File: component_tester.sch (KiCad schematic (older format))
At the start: 71 parts, among them IC1 ATMEGA16U2, IC2 ATMEGA328P-A, P1 USB_OTG, P10 BO_PC5, P11 ICSP_prog_328p, P12 CONN_01X01, P13 Device Under Test, P2 BATTERY_CONNECTOR, P3 Voltage_for_zener, P4 ICSP_prog_16u2, P5 BO_PC7, P6 BO_PD0, P7 BO_PD1, P8 BO_PC4, P9 BO_PC6, Q1 TRANSISTOR_NPN_2N2222_KSP222A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, SW1 SWITCH_DPDT_GROUNDED_BODY, SW2 DO_MEASUREMENT, SW3 CONNECT_CAP, U1 NCP1117ST50T3G, U2 XF2L-2625-1A, U3 CDSOT23-SRV05-4, U4 LT1004, Y1 8MHz, Y2 16MHz

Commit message: PCB drawn
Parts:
- removed C12: 100n, Capacitors_SMD:C_0805_HandSoldering, symbol C
- added F1, F2: FUSE, Resistors_SMD:R_0805_HandSoldering, symbol FUSE
- added P12: BO_PD2, Pin_Headers:Pin_Header_Straight_1x01, symbol CONN_01X01
- added P13: BO_PD3, Pin_Headers:Pin_Header_Straight_1x01, symbol CONN_01X01
- added P14: BO_PD4, Pin_Headers:Pin_Header_Straight_1x01, symbol CONN_01X01
- added P15: BO_PD5, Pin_Headers:Pin_Header_Straight_1x01, symbol CONN_01X01
- added P16: BO_PD6, Pin_Headers:Pin_Header_Straight_1x01, symbol CONN_01X01
- D1, D2: footprint Diodes_SMD:SOD-323 -> TO_SOT_Packages_SMD:SOT-23
- D3: renamed from D4; footprint Diodes_SMD:SOD-323 -> TO_SOT_Packages_SMD:SOT-23
- D4: renamed from D5; footprint Diodes_SMD:SOD-323 -> TO_SOT_Packages_SMD:SOT-23
- D7: renamed from D6; footprint Diodes_SMD:SOD-323 -> TO_SOT_Packages_SMD:SOT-23
- SW1: value SWITCH_DPDT_GROUNDED_BODY -> ON-OFF switch
- renumbered C6 to C11, C17 to C16, C18 to C17, C19 to C18, C16 to C19, C8 to C4, C4 to C5, C5 to C6, C11 to C8, D3 to D5, D7 to D6, P12 to P17, P13 to P18, R15 to R14, R14 to R15, R17 to R16, R16 to R17, R6 to R3, R3 to R4, R4 to R5, R5 to R6, U4 to U3, U3 to U4
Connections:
- net 5Volt_328: now also F1.2; no longer SW1.1
- net Battery_input: now also SW1.5, F2.2; no longer C8.1, D3.1 (K), D4.1 (K), R1.1, SW1.6
- net GND: now also C16.1, C17.1, C8.2, D4.2 (A)
- net USB_Vcc: now also SW1.3; no longer SW1.2
- net Volt_reg_5v: now also SW1.2; no longer SW1.3
- net control-niet_data-wel: now also IC1.12 ((~RTS~/AIN5/INT6)PD6); no longer IC1.10 ((INT5/AIN3)PD4)
- net lcd_reset-niet: now also IC1.10 ((INT5/AIN3)PD4); no longer IC1.12 ((~RTS~/AIN5/INT6)PD6)
- net at IC2.1 ((PCINT19/OC2B/INT1)PD3): now also P13.1 (P1)
- net at IC2.10 ((PCINT22/OC0A/AIN0)PD6): now also P16.1 (P1)
- net at IC2.2 ((PCINT20/XCK/T0)PD4): now also P14.1 (P1)
- net at IC2.32 ((PCINT18/INT0)PD2): now also P12.1 (P1)
- net at IC2.9 ((PCINT21/OC0B/T1)PD5): now also P15.1 (P1)
- net Batt_Switch: now reaches C5.1, SW1.4, U1.3 (VI)
- net Batt_Switch: now also R1.1
- new net: F1.1, SW1.1
- new net: C8.1, D3.1 (K), D4.1 (K), F2.1
- no-connect marks 16 -> 11
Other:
- note added: "Optional battery charging circuit"
- note added: "Over voltage protection for test pins"
- moved on the sheet: C11, C19, C4, C8, D3, D4, D6, D7, L1, Q1, R1, R15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

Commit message: Updated schematic. New PCB layout.
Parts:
- added P19: DUT_SMD_1_2, Resistors_Universal:Resistor_SMDuniversal_0805to2512_HandSoldering, symbol CONN_01X02
- added P20: DUT_SMD_2_3, Resistors_Universal:Resistor_SMDuniversal_0805to2512_HandSoldering, symbol CONN_01X02
- C18: footprint Capacitors_SMD:C_0805_HandSoldering -> Capacitors_ThroughHole:C_Disc_D3_P2.5
- P18: footprint Pin_Headers:Pin_Header_Straight_1x03 -> drawn_by_jpmeijers:CONN_DUT
- R11, R12, R13, R14, R16, R18: footprint Resistors_SMD:R_0805_HandSoldering -> Resistors_ThroughHole:Resistor_Horizontal_RM10mm
- Y1, Y2: footprint Crystals:Crystal_HC49-U_Vertical -> Crystals:Crystal_HC49-SD_SMD
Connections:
- net DUT1: now also P19.2 (P2)
- net DUT2: now also P19.1 (P1), P20.2 (P2)
- net DUT3: now also P20.1 (P1)
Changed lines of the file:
@@
 F 0 "P18" H 13050 5000 50  0000 C CNN
 F 1 "Device Under Test" V 13150 4800 50  0000 C CNN
-F 2 "Pin_Headers:Pin_Header_Straight_1x03" H 13050 4800 50  0001 C CNN
+F 2 "drawn_by_jpmeijers:CONN_DUT" H 13050 4800 50  0001 C CNN
 F 3 "" H 13050 4800 50  0000 C CNN
 	1    13050 4800
@@
 F 0 "R11" V 10830 3850 50  0000 C CNN
 F 1 "680" V 10750 3850 50  0000 C CNN
-F 2 "Resistors_SMD:R_0805_HandSoldering" V 10680 3850 50  0001 C CNN
+F 2 "Resistors_ThroughHole:Resistor_Horizontal_RM10mm" V 10680 3850 50  0001 C CNN
 F 3 "" H 10750 3850 50  0000 C CNN
 	1    10750 3850
@@
 F 0 "R12" V 10925 3950 50  0000 C CNN
 F 1 "470k" V 11000 3950 50  0000 C CNN
-F 2 "Resistors_SMD:R_0805_HandSoldering" V 10930 3950 50  0001 C CNN
+F 2 "Resistors_ThroughHole:Resistor_Horizontal_RM10mm" V 10930 3950 50  0001 C CNN
 F 3 "" H 11000 3950 50  0000 C CNN
 	1    11000 3950
@@
 F 0 "R14" V 11580 4150 50  0000 C CNN
 F 1 "470k" V 11500 4150 50  0000 C CNN
-F 2 "Resistors_SMD:R_0805_HandSoldering" V 11430 4150 50  0001 C CNN
+F 2 "Resistors_ThroughHole:Resistor_Horizontal_RM10mm" V 11430 4150 50  0001 C CNN
 F 3 "" H 11500 4150 50  0000 C CNN
 	1    11500 4150
@@
 F 0 "R13" V 11330 4050 50  0000 C CNN
 F 1 "680" V 11250 4050 50  0000 C CNN
-F 2 "Resistors_SMD:R_0805_HandSoldering" V 11180 4050 50  0001 C CNN
+F 2 "Resistors_ThroughHole:Resistor_Horizontal_RM10mm" V 11180 4050 50  0001 C CNN
 F 3 "" H 11250 4050 50  0000 C CNN
 	1    11250 4050
@@
 F 0 "R16" V 11830 4250 50  0000 C CNN
 F 1 "680" V 11750 4250 50  0000 C CNN
-F 2 "Resistors_SMD:R_0805_HandSoldering" V 11680 4250 50  0001 C CNN
+F 2 "Resistors_ThroughHole:Resistor_Horizontal_RM10mm" V 11680 4250 50  0001 C CNN
 F 3 "" H 11750 4250 50  0000 C CNN
 	1    11750 4250
@@
 F 0 "R18" V 12080 4350 50  0000 C CNN
 F 1 "470k" V 12000 4350 50  0000 C CNN
-F 2 "Resistors_SMD:R_0805_HandSoldering" V 11930 4350 50  0001 C CNN
+F 2 "Resistors_ThroughHole:Resistor_Horizontal_RM10mm" V 11930 4350 50  0001 C CNN
 F 3 "" H 12000 4350 50  0000 C CNN
 	1    12000 4350
@@
 F 0 "Y2" V 10775 4400 50  0000 C CNN
 F 1 "16MHz" V 10700 4350 50  0000 C CNN
-F 2 "Crystals:Crystal_HC49-U_Vertical" H 10750 4525 50  0001 C CNN
+F 2 "Crystals:Crystal_HC49-SD_SMD" H 10750 4525 50  0001 C CNN
 F 3 "" H 10750 4525 50  0000 C CNN
 	1    10750 4525
@@
 F 0 "Y1" H 2575 3200 50  0000 C CNN
 F 1 "8MHz" H 2575 3000 50  0000 C CNN
-F 2 "Crystals:Crystal_HC49-U_Vertical" H 2575 3100 50  0001 C CNN
+F 2 "Crystals:Crystal_HC49-SD_SMD" H 2575 3100 50  0001 C CNN
 F 3 "" H 2575 3100 50  0000 C CNN
 	1    2575 3100
@@
 F 0 "C18" H 14000 4800 50  0000 L CNN
 F 1 "22nF high quality" H 14000 4600 50  0000 L CNN
-F 2 "Capacitors_SMD:C_0805_HandSoldering" H 14013 4550 50  0001 C CNN
+F 2 "Capacitors_ThroughHole:C_Disc_D3_P2.5" H 14013 4550 50  0001 C CNN
 F 3 "" H 13975 4700 50  0000 C CNN
 	1    13975 4700
@@
 	11125 4525 11100 4525
 Connection ~ 11100 4525
+$Comp
+L CONN_01X02 P19
+U 1 1 5769C94E
+P 14100 5825
+F 0 "P19" H 14100 5975 50  0000 C CNN
+F 1 "DUT_SMD_1_2" H 14400 5825 50  0000 C CNN
+F 2 "Resistors_Universal:Resistor_SMDuniversal_0805to2512_HandSoldering" V 14725 5825 50  0001 C CNN
+F 3 "" H 14100 5825 50  0000 C CNN
+	1    14100 5825
+	0    1    1    0
+$EndComp
+$Comp
+L CONN_01X02 P20
+U 1 1 5769CA3D
+P 14550 5825
+F 0 "P20" H 14550 5975 50  0000 C CNN
+F 1 "DUT_SMD_2_3" H 14850 5825 50  0000 C CNN
+F 2 "Resistors_Universal:Resistor_SMDuniversal_0805to2512_HandSoldering" V 15275 5825 50  0001 C CNN
+F 3 "" H 14550 5825 50  0000 C CNN
+	1    14550 5825
+	0    1    1    0
+$EndComp
+Text Label 14050 5625 1    60   ~ 0
+DUT1
+Text Label 14150 5625 1    60   ~ 0
+DUT2
+Text Label 14500 5625 1    60   ~ 0
+DUT2
+Text Label 14600 5625 1    60   ~ 0
+DUT3
 $EndSCHEMATC

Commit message: Version 3 of the PCB
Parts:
- removed P11: ICSP_prog_328p, Pin_Headers:Pin_Header_Straight_2x03, symbol CONN_02X03
- removed P19: DUT_SMD_1_2, Resistors_Universal:Resistor_SMDuniversal_0805to2512_HandSoldering, symbol CONN_01X02
- removed P20: DUT_SMD_2_3, Resistors_Universal:Resistor_SMDuniversal_0805to2512_HandSoldering, symbol CONN_01X02
- removed P4: ICSP_prog_16u2, Pin_Headers:Pin_Header_Straight_2x03, symbol CONN_02X03
- added C19: 100n, Capacitors_SMD:C_0805_HandSoldering, symbol C_Small
- added P10: ICSP_prog_16u2_4, Pin_Headers:Pin_Header_Straight_1x01, symbol CONN_01X01
- added P12: ICSP_prog_16u2_5, Pin_Headers:Pin_Header_Straight_1x01, symbol CONN_01X01
- added P19: ICSP_prog_328_1, Pin_Headers:Pin_Header_Straight_1x01, symbol CONN_01X01
- added P20: ICSP_prog_328_3, Pin_Headers:Pin_Header_Straight_1x01, symbol CONN_01X01
- added P21: ICSP_prog_328_4, Pin_Headers:Pin_Header_Straight_1x01, symbol CONN_01X01
- added P22: ICSP_prog_328_5, Pin_Headers:Pin_Header_Straight_1x01, symbol CONN_01X01
- added P25: CONN_01X03, drawn_by_jpmeijers:CONN_DUT_SMD, symbol CONN_01X03
- added P5: ICSP_prog_16u2_1, Pin_Headers:Pin_Header_Straight_1x01, symbol CONN_01X01
- added P9: ICSP_prog_16u2_3, Pin_Headers:Pin_Header_Straight_1x01, symbol CONN_01X01
- Q1: footprint TO_SOT_Packages_THT:TO-92_Rugged -> TO_SOT_Packages_THT:TO-92_Inline_Narrow_Oval
- R11, R12, R13, R14, R16, R18: footprint Resistors_ThroughHole:Resistor_Horizontal_RM10mm -> Resistors_SMD:R_0805_HandSoldering
- U2: footprint drawn_by_jpmeijers:XF2L-2625-1A -> drawn_by_jpmeijers:CONN_FPC_FFC_0.5mm_26PIN_DRAWER_BOTTOM
- Y1, Y2: footprint Crystals:Crystal_HC49-SD_SMD -> Crystals:Crystal_HC49-U_Vertical
- renumbered C13 to C12, C14 to C13, C15 to C14, C16 to C15, C17 to C16, C18 to C17, C19 to C18, F2 to F1, F1 to F2, P9 to P11, P10 to P13, P12 to P14, P13 to P15, P14 to P16, P15 to P17, P16 to P18, P17 to P23, P18 to P24, P5 to P4, R3 to R1, R4 to R2, R5 to R3, R6 to R4, R1 to R5, R2 to R6
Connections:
- net 5Volt_328: now also SW1.1, C19.1; no longer F2.2
- net Battery_input: now also F2.1; no longer F1.2, P3.1 (P1), SW1.5
- net DUT1: now also P25.1 (P1)
- net DUT2: now also P25.2 (P2)
- net DUT3: now also P25.3 (P3)
- net GND: now also C19.2
- net LCD_DATA_B1: now also P9.1 (P1)
- net LCD_DATA_B2: now also P10.1 (P1)
- net LCD_DATA_B3: now also P5.1 (P1)
- net RESET_16u: now also P12.1 (P1)
- net RESET_328: now also P22.1 (P1)
- net USB_Vcc: now also F1.2; no longer P1.1 (VCC)
- net 328_MOSI: now reaches IC2.15 ((PCINT3/OC2A/MOSI)PB3), R14.2
- net 328_MOSI: now also P21.1 (P1)
- net 328_MISO: now reaches IC2.16 ((PCINT4/MISO)PB4), R16.2
- net 328_MISO: now also P19.1 (P1)
- net 328_SCK: now reaches IC2.17 ((PCINT5/SCK)PB5), R18.2
- net 328_SCK: now also P20.1 (P1)
- net Battery_fused: now reaches C8.1, D3.1 (K), D4.1 (K)
- net Battery_fused: now also F2.2, P3.1 (P1), SW1.5; no longer F1.1
- new net: F1.1, P1.1 (VCC)
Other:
- moved on the sheet: F1, F2, P3

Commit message: Resonator Capacitor closer. A lot of GND vias.
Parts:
- C17: footprint Capacitors_ThroughHole:C_Disc_D3_P2.5 -> Capacitors_SMD:C_1206_HandSoldering
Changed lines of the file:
@@
 F 0 "C17" H 14000 4800 50  0000 L CNN
 F 1 "22nF high quality" H 14000 4600 50  0000 L CNN
-F 2 "Capacitors_ThroughHole:C_Disc_D3_P2.5" H 14013 4550 50  0001 C CNN
+F 2 "Capacitors_SMD:C_1206_HandSoldering" H 14013 4550 50  0001 C CNN
 F 3 "" H 13975 4700 50  0000 C CNN
 	1    13975 4700

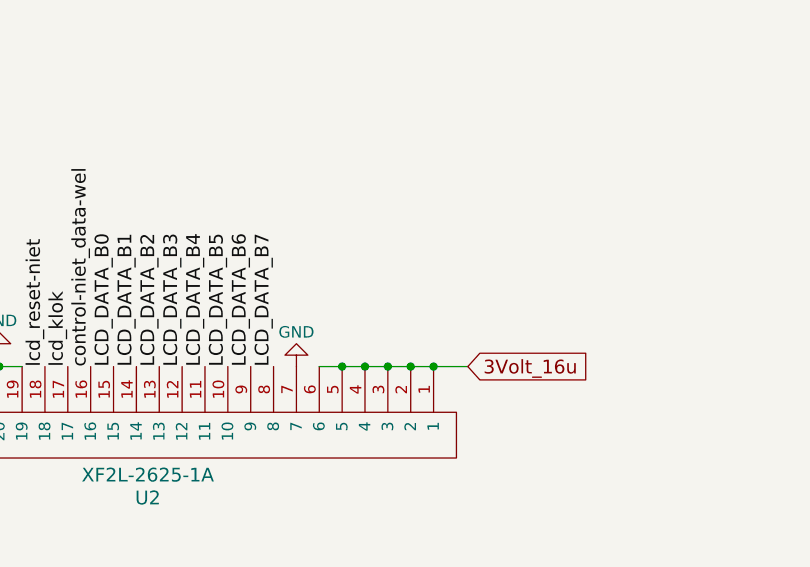
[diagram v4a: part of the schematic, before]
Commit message: Added extra vias. Add cap on LCD power.
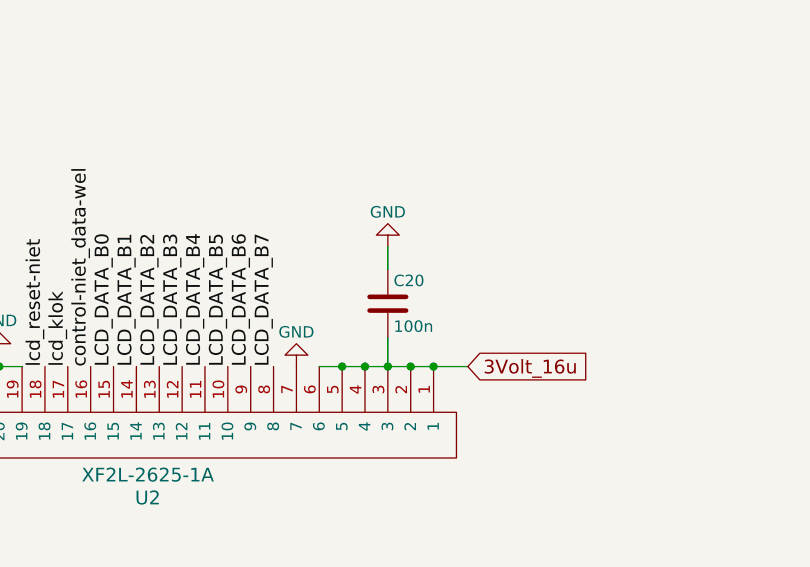
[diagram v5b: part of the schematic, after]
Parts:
- added C20: 100n, Capacitors_SMD:C_0805_HandSoldering, symbol C
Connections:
- net 3Volt_16u: now also C20.2
- net GND: now also C20.1
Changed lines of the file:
@@
 Wire Wire Line
 	8225 4150 8225 3850
+$Comp
+L C C20
+U 1 1 576B1733
+P 9950 8625
+F 0 "C20" H 9975 8725 50  0000 L CNN
+F 1 "100n" H 9975 8525 50  0000 L CNN
+F 2 "Capacitors_SMD:C_0805_HandSoldering" H 9988 8475 50  0001 C CNN
+F 3 "" H 9950 8625 50  0000 C CNN
+	1    9950 8625
+	1    0    0    -1
+$EndComp
+$Comp
+L GND #PWR035
+U 1 1 576B1814
+P 9950 8375
+F 0 "#PWR035" H 9950 8125 50  0001 C CNN
+F 1 "GND" H 9950 8225 50  0000 C CNN
+F 2 "" H 9950 8375 50  0000 C CNN
+F 3 "" H 9950 8375 50  0000 C CNN
+	1    9950 8375
+	-1   0    0    1
+$EndComp
+Wire Wire Line
+	9950 8375 9950 8475
+Wire Wire Line
+	9950 8775 9950 8900
 $EndSCHEMATC

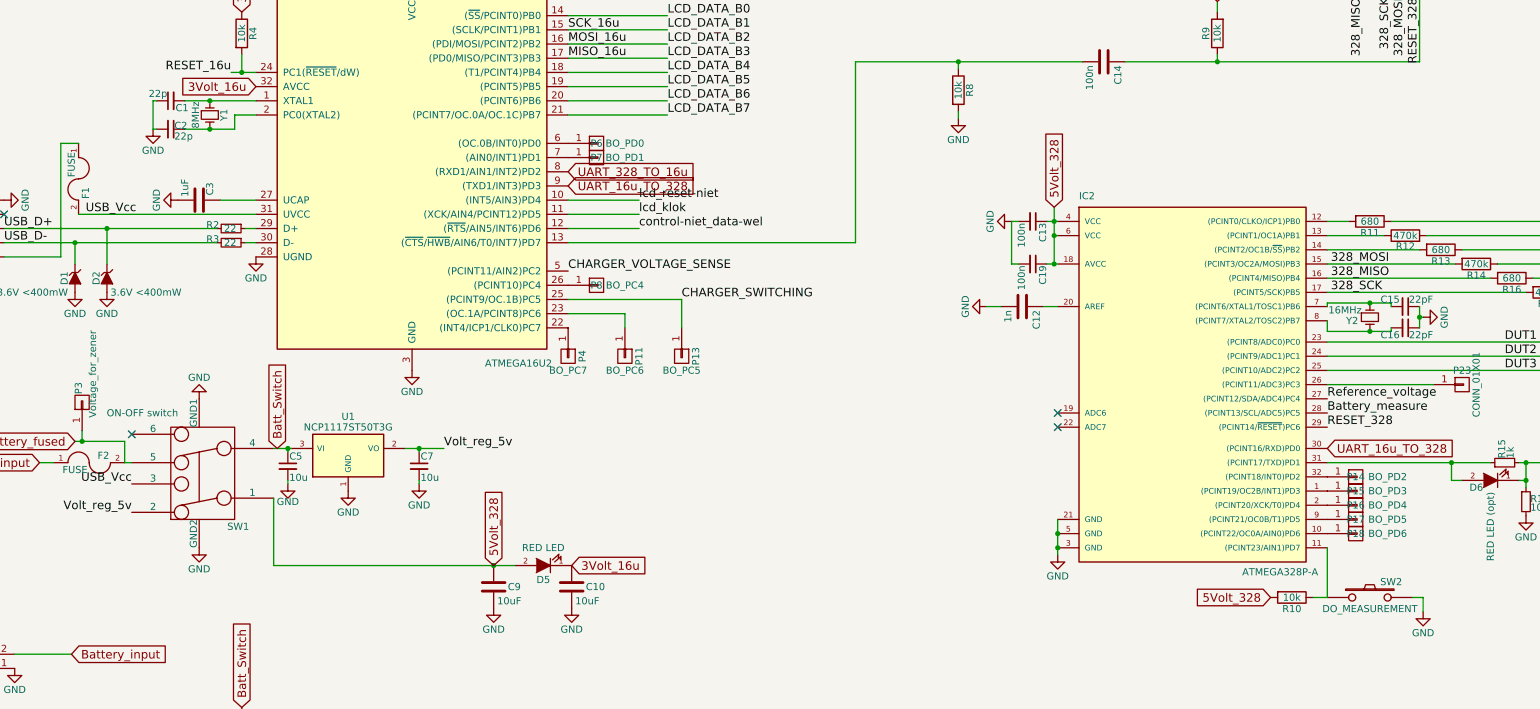
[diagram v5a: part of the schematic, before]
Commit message: Fix capacitor values Added Vusb cap, fix unconnected nets, better grounding.
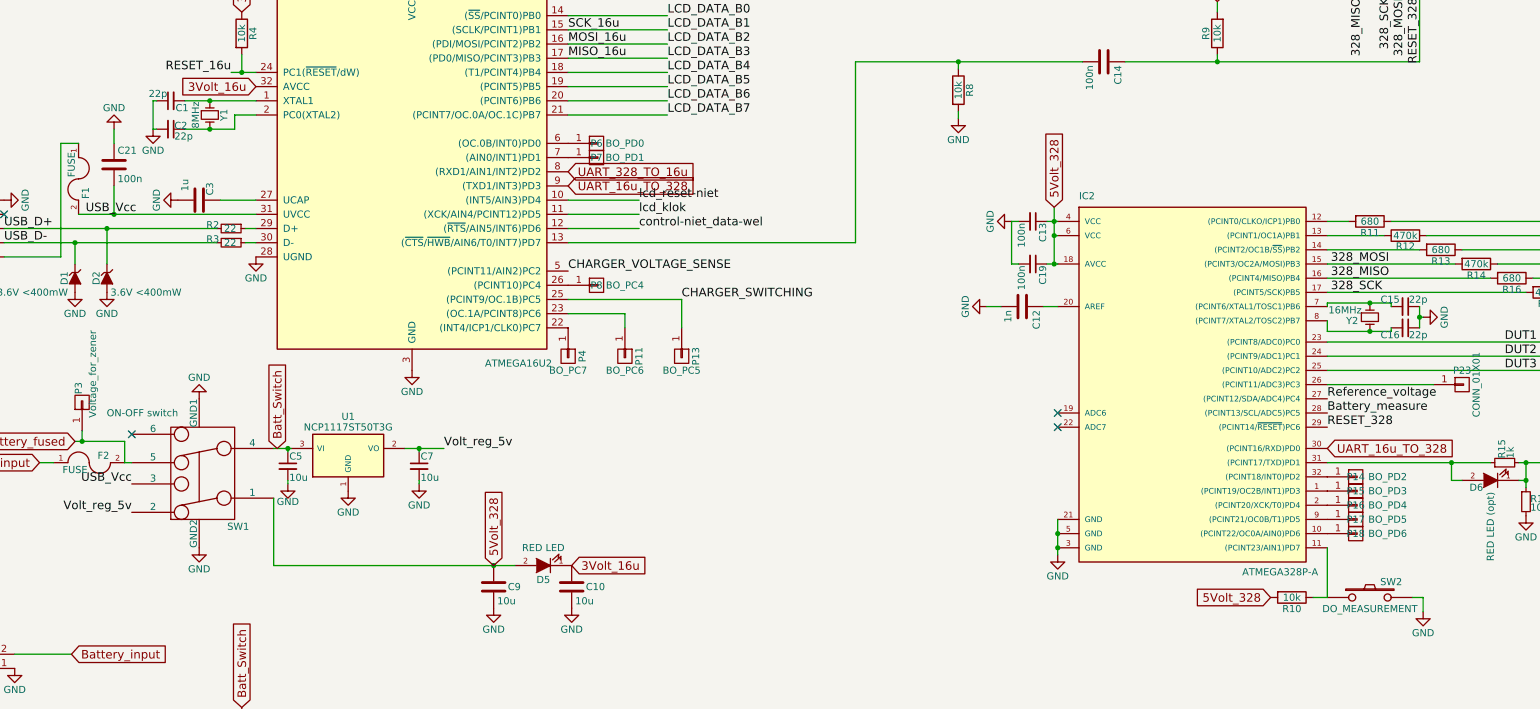
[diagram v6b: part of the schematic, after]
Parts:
- added C21: 100n, Capacitors_SMD:C_0805_HandSoldering, symbol C
- C10, C9: value 10uF -> 10u
- C15, C16: value 22pF -> 22p
- C3: value 1uF -> 1u
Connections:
- net GND: now also C21.1
- net USB_Vcc: now also C21.2
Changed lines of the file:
@@
 P 11000 4600
 F 0 "C16" V 11050 4425 50  0000 L CNN
-F 1 "22pF" V 11050 4625 50  0000 L CNN
+F 1 "22p" V 11050 4625 50  0000 L CNN
 F 2 "Capacitors_SMD:C_0805_HandSoldering" H 11000 4600 50  0001 C CNN
 F 3 "" H 11000 4600 50  0000 C CNN
@@
 P 11000 4450
 F 0 "C15" V 10950 4275 50  0000 L CNN
-F 1 "22pF" V 10950 4475 50  0000 L CNN
+F 1 "22p" V 10950 4475 50  0000 L CNN
 F 2 "Capacitors_SMD:C_0805_HandSoldering" H 11000 4450 50  0001 C CNN
 F 3 "" H 11000 4450 50  0000 C CNN
@@
 P 2500 3700
 F 0 "C3" H 2375 3775 50  0000 L CNN
-F 1 "1uF" H 2350 3600 50  0000 L CNN
+F 1 "1u" H 2350 3600 50  0000 L CNN
 F 2 "Capacitors_SMD:C_0805_HandSoldering" H 2538 3550 50  0001 C CNN
 F 3 "" H 2500 3700 50  0000 C CNN
@@
 P 4575 6425
 F 0 "C9" H 4675 6425 50  0000 L CNN
-F 1 "10uF" H 4600 6325 50  0000 L CNN
+F 1 "10u" H 4600 6325 50  0000 L CNN
 F 2 "Capacitors_SMD:C_0805_HandSoldering" H 4613 6275 50  0001 C CNN
 F 3 "" H 4575 6425 50  0000 C CNN
@@
 P 5125 6425
 F 0 "C10" H 5225 6425 50  0000 L CNN
-F 1 "10uF" H 5150 6325 50  0000 L CNN
+F 1 "10u" H 5150 6325 50  0000 L CNN
 F 2 "Capacitors_SMD:C_0805_HandSoldering" H 5163 6275 50  0001 C CNN
 F 3 "" H 5125 6425 50  0000 C CNN
@@
 Wire Wire Line
 	9950 8775 9950 8900
+$Comp
+L C C21
+U 1 1 576E82D6
+P 1900 3450
+F 0 "C21" H 1925 3550 50  0000 L CNN
+F 1 "100n" H 1925 3350 50  0000 L CNN
+F 2 "Capacitors_SMD:C_0805_HandSoldering" H 1938 3300 50  0001 C CNN
+F 3 "" H 1900 3450 50  0000 C CNN
+	1    1900 3450
+	1    0    0    -1
+$EndComp
+$Comp
+L GND #PWR036
+U 1 1 576E83D7
+P 1900 3200
+F 0 "#PWR036" H 1900 2950 50  0001 C CNN
+F 1 "GND" H 1900 3050 50  0000 C CNN
+F 2 "" H 1900 3200 50  0000 C CNN
+F 3 "" H 1900 3200 50  0000 C CNN
+	1    1900 3200
+	-1   0    0    1
+$EndComp
+Wire Wire Line
+	1900 3300 1900 3200
+Wire Wire Line
+	1900 3600 1900 3800
+Connection ~ 1900 3800
 $EndSCHEMATC
